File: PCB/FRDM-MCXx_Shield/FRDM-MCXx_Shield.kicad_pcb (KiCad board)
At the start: 4 copper layers, 91.4 x 54.6 mm, 114 parts, among them J2 Conn_01x04_Pin, J3 Conn_01x04_Pin, J4 Conn_01x03_Pin, J5 Conn_01x04_Pin, J6 Conn_01x04_Socket, J7 Conn_01x06_Socket, M1 Motor_Servo, SW1 PEC11L-4120F-N0020, SW2 SW_Push, SW3 SW_Push, U1 M95010-RMN6TP, U2 FXLS8974CF, U4 SN74LV164ADR

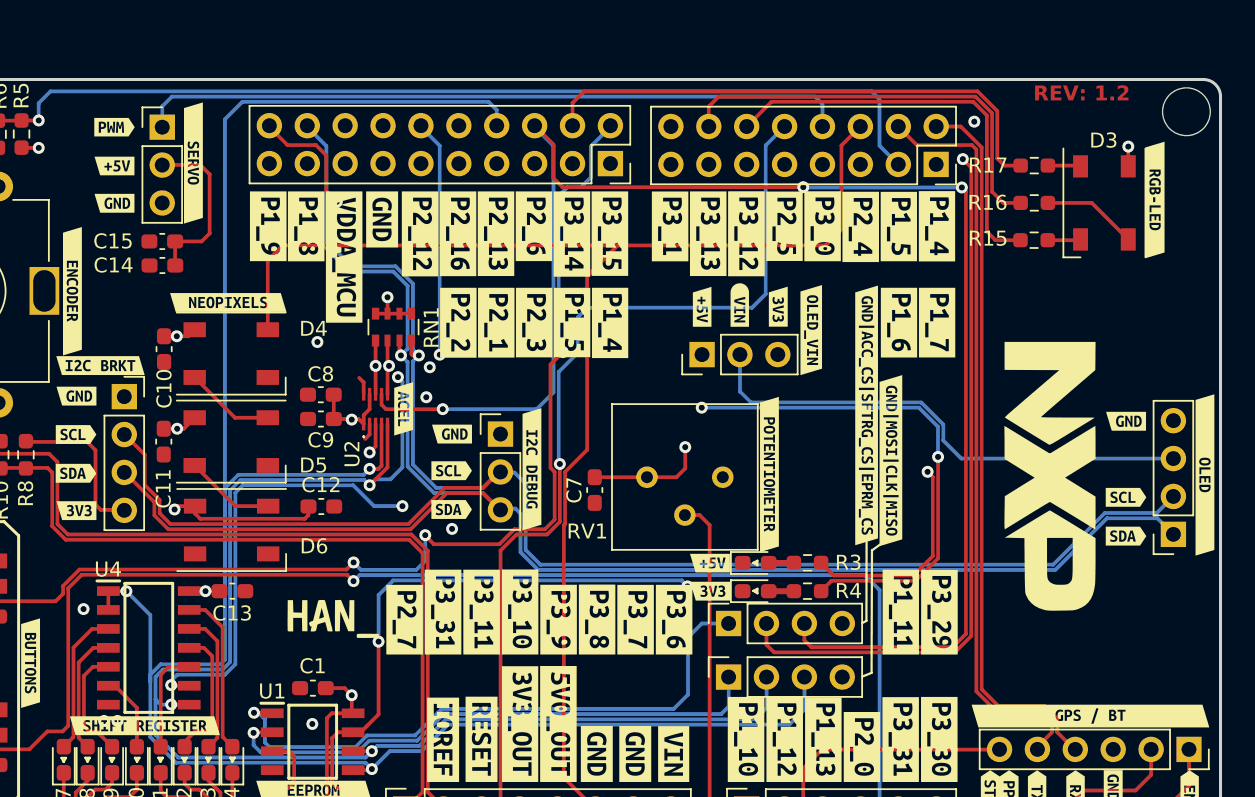
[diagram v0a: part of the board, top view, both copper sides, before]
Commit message: Updated PCB and added bill of materials
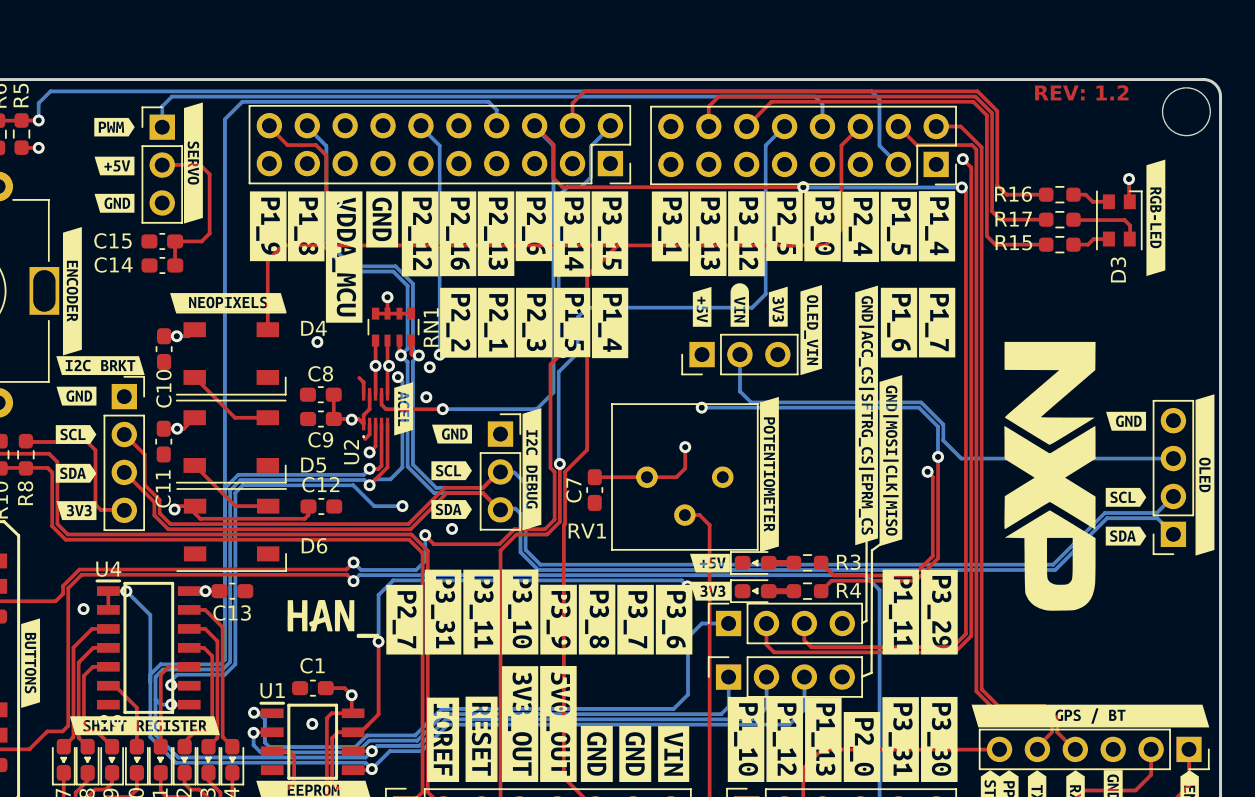
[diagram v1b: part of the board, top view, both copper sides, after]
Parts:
- C14: value 100uF -> 10uF
- D3: footprint LED_SMD:LED_SK6812_PLCC4_5.0x5.0mm_P3.2mm -> LED_SMD:LED_Cree-PLCC4_3.2x2.8mm_CCW
- J4: footprint Connector_PinHeader_2.54mm:PinHeader_1x03_P2.54mm_Vertical -> Connector_PinSocket_2.54mm:PinSocket_1x03_P2.54mm_Vertical
- R15, R16, R17, R3, RN2, RN3: value 420 -> 430
- R4: value 640 -> 680
- moved R17 4.01 mm to (184.9, 68.5)
- moved R16 1.80 mm to (184.9, 66.8)
- moved R15 1.75 mm to (184.9, 70.2)
- moved D3 1.54 mm to (188.8, 68.5)
- moved kibuzzard-65D74BEE 1.20 mm to (191.3, 68.4)
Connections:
- D3 pad 1: Net-(D3-RK) -> +3.3V
- D3 pad 3: +3.3V -> Net-(D3-RK)
- J1 pad B4: /LED_B -> /LED_G
- J1 pad D14: /LED_G -> /LED_B
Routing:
- net /LED_G: track 28.5 -> 39.4 mm
- net /LED_B: track 35.9 -> 31.5 mm
- net Net-(D3-GK): track 6.40 -> 2.70 mm
- net Net-(D3-BK): track 2.14 -> 4.93 mm
- net /LED_R: track 27.4 -> 29.5 mm
- net +3.3V: track 407.2 -> 406.2 mm
- net GND: vias 9 -> 8

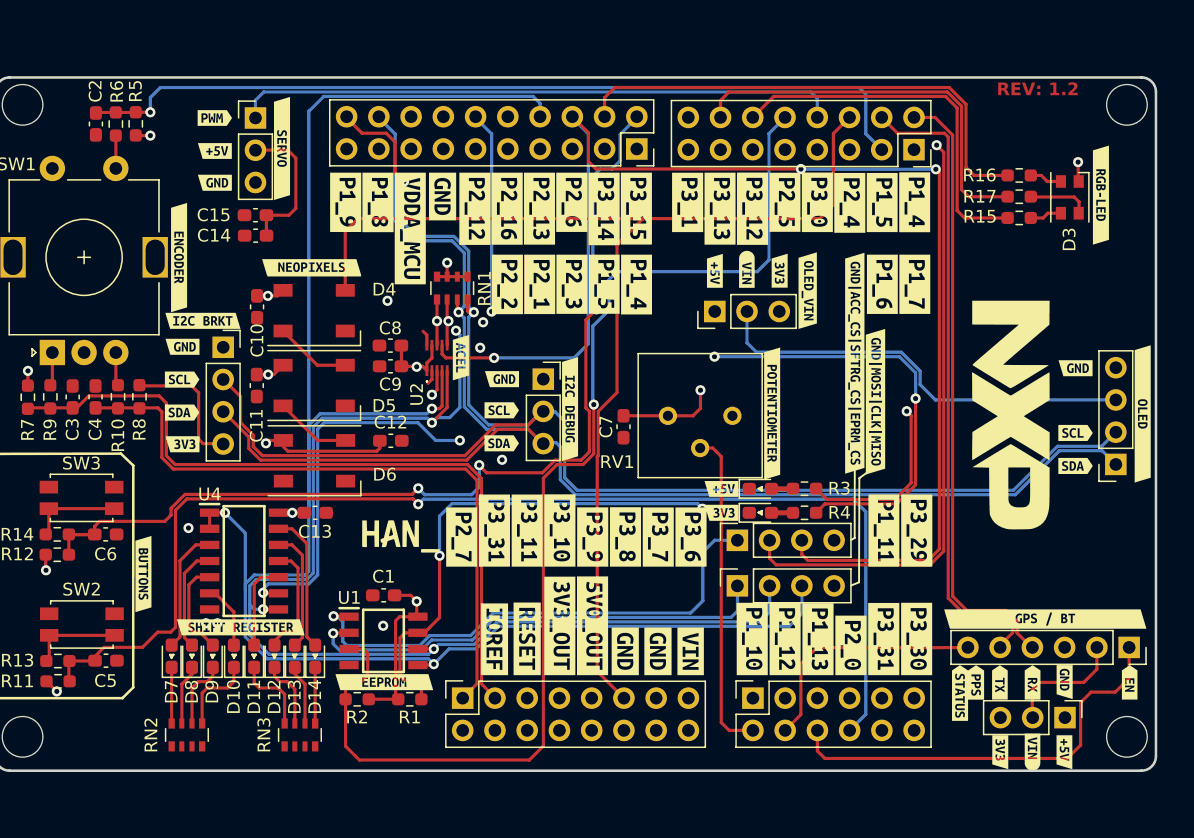
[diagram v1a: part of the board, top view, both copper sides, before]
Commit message: Updated trace spacing and pinout
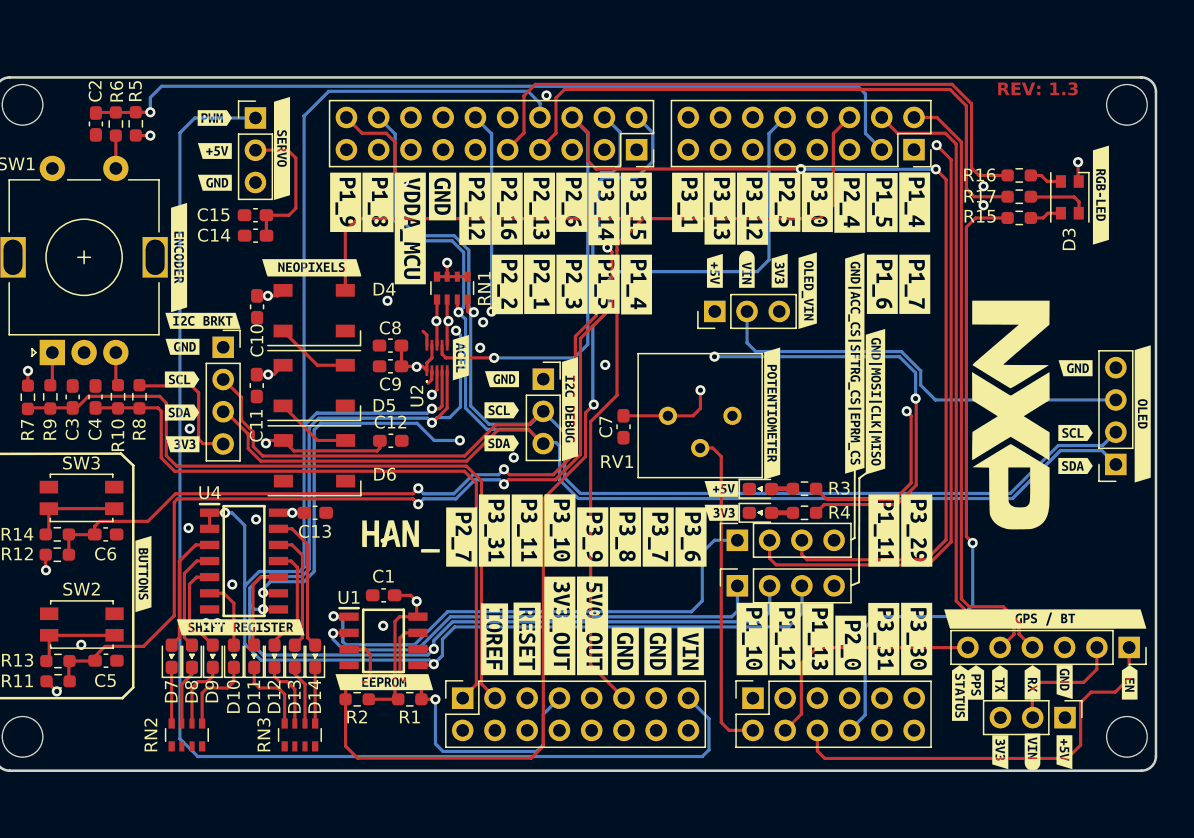
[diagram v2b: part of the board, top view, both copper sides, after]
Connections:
- J1 pad A15: unconnected-(J1A-P3_6-PadA15) -> /SERVO_PWM
- J1 pad A7: unconnected-(J1A-P3_10-PadA7) -> /~{HOLD}
- J1 pad B2: /SWITCH2 -> /SWITCH1
- J1 pad B4: /LED_G -> /SWITCH2
- J1 pad B7: unconnected-(J1B-P2_1-PadB7) -> /LED_B
- J1 pad B9: unconnected-(J1B-P2_2-PadB9) -> /LED_G
- J1 pad C8: /SWITCH1 -> /LED_R
- J1 pad D1: /~{HOLD} -> unconnected-(J1D-P1_7-PadD1)
- J1 pad D12: /LED_R -> unconnected-(J1D-P3_12-PadD12)
- J1 pad D14: /LED_B -> unconnected-(J1D-P3_13-PadD14)
- J1 pad D8: /SERVO_PWM -> unconnected-(J1D-P3_0-PadD8)
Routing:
- net /~{HOLD}: track 81.8 -> 25.5 mm, vias 2 -> 1
- net /SERVO_PWM: track 47.6 -> 101.4 mm
- net /LED_R: track 29.5 -> 51.4 mm, vias 0 -> 1
- net /LED_B: track 31.5 -> 47.7 mm
- net /LED_G: track 39.4 -> 49.1 mm
- net /SWITCH1: track 93.7 -> 86.6 mm, vias 1 -> 3
- net /SPI_MOSI: track 145.8 -> 140.2 mm
- net /SWITCH2: track 76.8 -> 74.4 mm
- net /WRITE_PROT: track 91.9 -> 90.8 mm
- net /SPI_CLK: track 112.7 -> 113.6 mm
- net /SCL: track 121.5 -> 121.0 mm
- net /ACC_INT2: track 69.9 -> 69.4 mm
- net GND: vias 8 -> 16
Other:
- board text added: "REV: 1.3"
- board text removed: "REV: 1.2"

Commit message: Updated V2.0
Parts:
- removed the C13 at (129.4, 93.4)
- removed C5, C6, C7: 100nF, Capacitor_SMD:C_0603_1608Metric_Pad1.08x0.95mm_HandSolder
- removed the C8 at (135.3, 80.2)
- removed the C9 at (135.3, 81.9)
- removed the D1 at (164.5, 91.5)
- removed D10, D11, D12, D13, D14, D7, D8, D9: LED, LED_SMD:LED_0603_1608Metric_Pad1.05x0.95mm_HandSolder
- removed the D2 at (164.5, 93.4)
- removed the D3 at (188.8, 68.5)
- removed the J7 at (193.5, 104.0)
- removed JP2: SolderJumper_3_Open, Connector_PinHeader_2.54mm:PinHeader_1x03_P2.54mm_Vertical
- removed R11, R12: 10k, Resistor_SMD:R_0603_1608Metric_Pad0.98x0.95mm_HandSolder
- removed R13, R14: 1k, Resistor_SMD:R_0603_1608Metric_Pad0.98x0.95mm_HandSolder
- removed R15, R16, R17: 430, Resistor_SMD:R_0603_1608Metric_Pad0.98x0.95mm_HandSolder
- removed the R3 at (167.9, 91.5)
- removed the R4 at (167.9, 93.4)
- removed RN1: 4.7k, Resistor_SMD:R_Array_Convex_4x0603
- removed RN2, RN3: 430, Resistor_SMD:R_Array_Convex_4x0603
- removed RV1: 5k, Potentiometer_THT:Potentiometer_Bourns_3386P_Vertical
- removed SW2, SW3: SW_Push, Button_Switch_SMD:SW_SPST_EVQP2
- removed U2: FXLS8974CF, SamacSys_Parts:FXLS8974CF
- removed U4: SN74LV164ADR, SamacSys_Parts:SOIC127P600X175-14N
- removed kibuzzard-65C7C6A4: G***, kibuzzard-65C7C6A4
- removed kibuzzard-65C7C6B6: G***, kibuzzard-65C7C6B6
- removed kibuzzard-65C7C6CC: G***, kibuzzard-65C7C6CC
- removed kibuzzard-65C7CAB6: G***, kibuzzard-65C7CAB6
- removed kibuzzard-65C7CCAF: G***, kibuzzard-65C7CCAF
- removed kibuzzard-65C7CD45: G***, kibuzzard-65C7CD45
- removed kibuzzard-65D5B8C7: G***, kibuzzard-65D5B8C7
- removed kibuzzard-65D5B8D9: G***, kibuzzard-65D5B8D9
- removed kibuzzard-65D5B8E6: G***, kibuzzard-65D5B8E6
- removed kibuzzard-65D5B934: G***, kibuzzard-65D5B934
- removed kibuzzard-65D5B943: G***, kibuzzard-65D5B943
- removed kibuzzard-65D5B980: G***, kibuzzard-65D5B980
- removed kibuzzard-65D5C5A7: G***, kibuzzard-65D5C5A7
- removed kibuzzard-65D5C99D: G***, kibuzzard-65D5C99D
- removed kibuzzard-65D74BEE: G***, kibuzzard-65D74BEE
- removed kibuzzard-65D74C28: G***, kibuzzard-65D74C28
- removed kibuzzard-65D9F210: G***, kibuzzard-65D9F210
- added J2: Conn_02x10_Odd_Even, Connector_PinHeader_2.54mm:PinHeader_2x10_P2.54mm_Vertical, B.Cu at (154.7, 64.8)
- added J3: Conn_02x06_Odd_Even, Connector_PinHeader_2.54mm:PinHeader_2x06_P2.54mm_Vertical, B.Cu at (163.9, 108.0)
- added J4: Conn_02x08_Odd_Even, Connector_PinHeader_2.54mm:PinHeader_2x08_P2.54mm_Vertical, B.Cu at (176.6, 64.8)
- added SSD1306: 128x64OLED, OLED:128x64OLED, F.Cu at (167.2, 82.2)
- added U3: 74HC595, Package_SO:TSSOP-16_4.4x5mm_P0.65mm, F.Cu at (223.0, 104.3)
- J1: value ~ -> Conn_02x08_Odd_Even; footprint User:MCX-A153_Shield_Template -> Connector_PinHeader_2.54mm:PinHeader_2x08_P2.54mm_Vertical; moved to B.Cu
- U1: footprint SamacSys_Parts:SOIC127P600X175-8N -> SamacSys:SOIC127P600X175-8N
- moved J1 54.4 mm to (141.0, 108.0), turned to -90 degrees
- moved REF** 17.0 mm to (174.0, 70.9)
- moved REF** 17.0 mm to (165.8, 70.8)
- renumbered C12 to C10, C14 to C12, C15 to C13, C10 to C8, C11 to C9, D4 to D1, D5 to D2, D6 to D3, J2 to J5, J3 to J6, J4 to J7, J5 to J8, J6 to J9, R5 to R3, R6 to R4, R7 to R5, R8 to R6, R9 to R7, R10 to R8
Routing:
- net +3.3V: track 405.9 -> 313.9 mm, vias 14 -> 8
- net /ACC_INT2: track 69.4 -> 0.00 mm, vias 1 -> 0
- net /ACC_INT1: track 69.4 -> 0.00 mm, vias 1 -> 0
- net +5V: track 184.0 -> 149.1 mm
- net /BT_EN: track 33.4 -> 21.6 mm
- net /Actuators/LED_H: track 11.0 -> 0.00 mm
- net /Actuators/LED_A: track 9.77 -> 0.00 mm
- net Net-(J7-Pin_2): track 9.68 -> 0.00 mm
- net /Actuators/LED_G: track 9.55 -> 0.00 mm
- net /Actuators/LED_F: track 8.67 -> 0.00 mm
- net /Actuators/LED_B: track 8.29 -> 0.00 mm
- net /SWITCH1: track 86.6 -> 78.5 mm
- net /RX: track 48.2 -> 40.5 mm
- net /Actuators/LED_C: track 7.68 -> 0.00 mm
- net /TX: track 50.3 -> 42.7 mm
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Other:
- board size 91.4 x 54.6 mm -> 51.1 x 54.7 mm
- board text added: "REV: 2.0"
- board text removed: "REV: 1.3"

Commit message: Updated PCB
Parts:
- removed C13: 100nF, Capacitor_SMD:C_0603_1608Metric_Pad1.08x0.95mm_HandSolder
- removed the J1 at (141.0, 108.0)
- removed the J3 at (163.9, 108.0)
- removed J9: Conn_01x04_Socket, Connector_PinSocket_2.54mm:PinSocket_1x04_P2.54mm_Vertical
- added C11: 100nF, Capacitor_SMD:C_0805_2012Metric_Pad1.18x1.45mm_HandSolder, F.Cu at (141.3, 110.0)
- added C5: 10nF, Capacitor_SMD:C_0805_2012Metric_Pad1.18x1.45mm_HandSolder, F.Cu at (157.5, 88.9)
- added C6: 100nF, Capacitor_SMD:C_0805_2012Metric_Pad1.18x1.45mm_HandSolder, F.Cu at (165.6, 102.7)
- added C7: 100nF, Capacitor_SMD:C_0805_2012Metric_Pad1.18x1.45mm_HandSolder, F.Cu at (172.2, 102.7)
- added D10: SP0503BAHT, Package_TO_SOT_SMD:SOT-143, B.Cu at (139.7, 80.0)
- added D11: SP0503BAHT, Package_TO_SOT_SMD:SOT-143, B.Cu at (148.4, 80.0)
- added D12: SP0503BAHT, Package_TO_SOT_SMD:SOT-143, F.Cu at (157.3, 101.6)
- added D13: SP0503BAHT, Package_TO_SOT_SMD:SOT-143, B.Cu at (152.9, 107.9)
- added D14: SK6812, LED_SMD:LED_SK6812_PLCC4_5.0x5.0mm_P3.2mm, F.Cu at (164.7, 107.5)
- added D15: SK6812, LED_SMD:LED_SK6812_PLCC4_5.0x5.0mm_P3.2mm, F.Cu at (171.3, 107.5)
- added D16: SK6812, LED_SMD:LED_SK6812_PLCC4_5.0x5.0mm_P3.2mm, F.Cu at (177.9, 107.5)
- added D4: LED, LED_SMD:LED_0805_2012Metric_Pad1.15x1.40mm_HandSolder, F.Cu at (179.5, 90.9)
- added D5: LED, LED_SMD:LED_0805_2012Metric_Pad1.15x1.40mm_HandSolder, F.Cu at (176.3, 98.7)
- added D6: LED, LED_SMD:LED_0805_2012Metric_Pad1.15x1.40mm_HandSolder, F.Cu at (168.5, 101.9)
- added D7: LED, LED_SMD:LED_0805_2012Metric_Pad1.15x1.40mm_HandSolder, F.Cu at (160.8, 98.7)
- added D8: LED, LED_SMD:LED_0805_2012Metric_Pad1.15x1.40mm_HandSolder, F.Cu at (157.5, 90.9)
- added D9: SP0503BAHT, Package_TO_SOT_SMD:SOT-143, B.Cu at (144.0, 80.0)
- added J2: Conn_02x06_Odd_Even, Connector_PinHeader_2.54mm:PinHeader_2x06_P2.54mm_Vertical, B.Cu at (163.7, 112.8)
- added J4: Conn_02x08_Odd_Even, Connector_PinHeader_2.54mm:PinHeader_2x08_P2.54mm_Vertical, B.Cu at (140.8, 112.8)
- added RN1: 4.7k, Resistor_SMD:R_Array_Convex_4x1206, F.Cu at (132.7, 81.6)
- added RN2: 1k, Resistor_SMD:R_Array_Convex_4x1206, F.Cu at (168.5, 75.5)
- added RN3: 1k, Resistor_SMD:R_Array_Convex_4x1206, F.Cu at (177.4, 75.5)
- added TP1: 5001, SamacSys:5000, F.Cu at (179.8, 68.1)
- added TP2: 5001, SamacSys:5000, F.Cu at (161.1, 102.0)
- added TP3: 5001, SamacSys:5000, F.Cu at (157.3, 82.3)
- added TP4: 5001, SamacSys:5000, F.Cu at (137.4, 106.9)
- added TP5: 5001, SamacSys:5000, F.Cu at (158.5, 105.0)
- added TP6: 5001, SamacSys:5000, F.Cu at (158.5, 109.4)
- added U2: M95010-RMN6TP, SamacSys:SOIC127P600X175-8N, F.Cu at (146.7, 74.5)
- C1, C2, C3, C8, C9: footprint Capacitor_SMD:C_0603_1608Metric_Pad1.08x0.95mm_HandSolder -> Capacitor_SMD:C_0805_2012Metric_Pad1.18x1.45mm_HandSolder
- C10: value 100nF -> 10uF; footprint Capacitor_SMD:C_0603_1608Metric_Pad1.08x0.95mm_HandSolder -> Capacitor_SMD:C_0805_2012Metric_Pad1.18x1.45mm_HandSolder
- C12: value 10uF -> 100nF; footprint Capacitor_SMD:C_0603_1608Metric_Pad1.08x0.95mm_HandSolder -> Capacitor_SMD:C_0805_2012Metric_Pad1.18x1.45mm_HandSolder
- C4: value 100nF -> 10nF; footprint Capacitor_SMD:C_0603_1608Metric_Pad1.08x0.95mm_HandSolder -> Capacitor_SMD:C_0805_2012Metric_Pad1.18x1.45mm_HandSolder
- D1, D2, D3: value SK6812 -> LED; footprint LED_SMD:LED_SK6812_PLCC4_5.0x5.0mm_P3.2mm -> LED_SMD:LED_0805_2012Metric_Pad1.15x1.40mm_HandSolder
- J5: value Conn_01x04_Pin -> Conn_01x04_Socket
- J6, J8: footprint Connector_PinSocket_2.54mm:PinSocket_1x04_P2.54mm_Vertical -> Connector_PinHeader_2.54mm:PinHeader_1x04_P2.54mm_Vertical
- J7: value Conn_01x03_Pin -> Conn_01x04_Pin; footprint Connector_PinSocket_2.54mm:PinSocket_1x03_P2.54mm_Vertical -> Connector_PinHeader_2.54mm:PinHeader_1x04_P2.54mm_Vertical
- JP1: footprint Connector_PinHeader_2.54mm:PinHeader_1x03_P2.54mm_Vertical -> Jumper:SolderJumper-3_P2.0mm_Open_TrianglePad1.0x1.5mm; moved to B.Cu
- R1, R3: footprint Resistor_SMD:R_0603_1608Metric_Pad0.98x0.95mm_HandSolder -> Resistor_SMD:R_0805_2012Metric_Pad1.20x1.40mm_HandSolder
- R2, R5, R6: value 10k -> 1k; footprint Resistor_SMD:R_0603_1608Metric_Pad0.98x0.95mm_HandSolder -> Resistor_SMD:R_0805_2012Metric_Pad1.20x1.40mm_HandSolder
- R4, R7, R8: value 1k -> 10k; footprint Resistor_SMD:R_0603_1608Metric_Pad0.98x0.95mm_HandSolder -> Resistor_SMD:R_0805_2012Metric_Pad1.20x1.40mm_HandSolder
- SW1: value PEC11L-4120F-N0020 -> EC12D1524406; footprint Rotary_Encoder:RotaryEncoder_Alps_EC11E-Switch_Vertical_H20mm -> SamacSys:EC12D1564404
- U1: value M95010-RMN6TP -> 74HC595; footprint SamacSys:SOIC127P600X175-8N -> Package_SO:TSSOP-16_4.4x5mm_P0.65mm
- U3: value 74HC595 -> LM35-D; footprint Package_SO:TSSOP-16_4.4x5mm_P0.65mm -> Package_SO:SOIC-8_3.9x4.9mm_P1.27mm
- moved kibuzzard-65C7C5A7 170.9 mm to (47.4, 177.2)
- moved kibuzzard-65C7C751 170.9 mm to (47.4, 182.3)
- moved kibuzzard-65C7C77A 170.9 mm to (47.4, 184.9)
- moved kibuzzard-65D9ED05 170.9 mm to (52.7, 180.8)
- moved kibuzzard-65D9F158 155.2 mm to (34.4, 156.7)
- moved kibuzzard-65C7C73C 155.2 mm to (29.3, 156.7)
- moved kibuzzard-65D9F1EE 155.2 mm to (31.8, 156.6)
- moved kibuzzard-65D9F4C2 155.2 mm to (36.6, 158.2)
- moved kibuzzard-65D9F92F 145.9 mm to (67.7, 183.7)
- moved kibuzzard-65D9F962 145.9 mm to (69.3, 186.7)
- moved kibuzzard-65C7C452 115.8 mm to (23.2, 123.4)
- moved kibuzzard-65C7C5C0 115.8 mm to (23.2, 126.0)
- moved kibuzzard-65C7C5CF 115.8 mm to (23.2, 128.5)
- moved kibuzzard-65C7CF1C 115.8 mm to (28.5, 125.8)
- moved kibuzzard-65C7C751 112.3 mm to (57.1, 156.3)
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- renumbered J4 to J1, J2 to J3
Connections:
- C10 pad 1: +3.3V -> GND
- C10 pad 2: GND -> +5V
- C12 pad 1: GND -> +3.3V
- C12 pad 2: +5V -> GND
- C2 pad 1: /ENC_SW -> GND
- C2 pad 2: GND -> +3.3V
- C3 pad 1: /ENC_A -> /ENC_SW
- C4 pad 1: /ENC_B -> /ENC_A
- D1 pad 2: /LED_NEOPIXEL -> Net-(D1-A)
- D2 pad 2: Net-(D1-DOUT) -> Net-(D2-A)
- D3 pad 2: Net-(D2-DOUT) -> Net-(D3-A)
- J1 pad 14: unconnected-(J4-Pin_14-Pad14) -> /SERVO_PWM
- J1 pad 16: /~{SHIFTREG_CS} -> /~{SHIFTREG_RST}
- J1 pad 2: /RX -> unconnected-(J1-Pin_2-Pad2)
- J1 pad 4: /TX -> unconnected-(J1-Pin_4-Pad4)
- J1 pad 6: /LED_NEOPIXEL -> unconnected-(J1-Pin_6-Pad6)
- J3 pad 2: /SWITCH1 -> unconnected-(J3-Pin_2-Pad2)
- J3 pad 3: /ACC_INT2 -> unconnected-(J3-Pin_3-Pad3)
- J3 pad 4: /SWITCH2 -> unconnected-(J3-Pin_4-Pad4)
- J3 pad 5: /ACC_INT1 -> unconnected-(J3-Pin_5-Pad5)
- J3 pad 6: /~{ACC_CS} -> /~{SHIFTREG_CS}
- J3 pad 7: /LED_B -> unconnected-(J3-Pin_7-Pad7)
- J3 pad 9: /LED_G -> unconnected-(J3-Pin_9-Pad9)
- J5 pad 1: /~{EEPROM_CS} -> /SDA
- J5 pad 2: /~{SHIFTREG_CS} -> /SCL
- J5 pad 3: /~{ACC_CS} -> Net-(J5-Pin_3)
- J6 pad 1: /SPI_MISO -> /~{EEPROM_CS}
- J6 pad 2: /SPI_CLK -> /~{SHIFTREG_CS}
- J6 pad 3: /SPI_MOSI -> /~{SHIFTREG_RST}
- J7 pad 1: GND -> /SPI_MOSI
- J7 pad 2: /SCL -> /SPI_CLK
- J7 pad 3: /SDA -> /SPI_MISO
- J8 pad 1: GND -> +3.3V
- J8 pad 2: /SCL -> /SDA
- J8 pad 3: /SDA -> /SCL
- J8 pad 4: +3.3V -> GND
- JP1 pad 1: +5V -> +3.3V
- JP1 pad 2: Net-(J9-Pin_3) -> Net-(J5-Pin_3)
- JP1 pad 3: +3.3V -> +5V
- R1 pad 1: +3.3V -> /ENC_SW
- R1 pad 2: /~{HOLD} -> +3.3V
- R2 pad 1: +3.3V -> /HMI/ENC_SW_RAW
- R2 pad 2: /WRITE_PROT -> /ENC_SW
- R3 pad 1: /ENC_SW -> /ENC_A
- R4 pad 1: /HMI/ENC_SW_RAW -> /ENC_B
- R4 pad 2: /ENC_SW -> +3.3V
- R5 pad 1: /ENC_A -> /HMI/ENC_A_RAW
- R5 pad 2: +3.3V -> /ENC_A
- R6 pad 1: /ENC_B -> /HMI/ENC_B_RAW
- R6 pad 2: +3.3V -> /ENC_B
- R7 pad 1: /HMI/ENC_A_RAW -> +3.3V
- R7 pad 2: /ENC_A -> Net-(U2-~{HOLD})
- R8 pad 1: /HMI/ENC_B_RAW -> +3.3V
- R8 pad 2: /ENC_B -> /WRITE_PROT
- U1 pad 1: /~{EEPROM_CS} -> Net-(RN2C-R3.2)
- U1 pad 2: /SPI_MISO -> Net-(RN2B-R2.2)
- U1 pad 3: /WRITE_PROT -> Net-(RN2A-R1.2)
- U1 pad 4: GND -> Net-(RN3A-R1.2)
- U1 pad 5: /SPI_MOSI -> Net-(RN3B-R2.2)
- U1 pad 6: /SPI_CLK -> Net-(RN3C-R3.2)
- U1 pad 7: /~{HOLD} -> Net-(RN3D-R4.2)
- U1 pad 8: +3.3V -> GND
- U3 pad 1: unconnected-(U3-QB-Pad1) -> /ADC_OUT
- U3 pad 4: unconnected-(U3-QE-Pad4) -> GND
- U3 pad 8: unconnected-(U3-GND-Pad8) -> +3.3V
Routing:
- net +3.3V: track 313.9 -> 37.0 mm, vias 8 -> 0
- net /~{SHIFTREG_CS}: track 143.5 -> 0.00 mm, vias 2 -> 0
- net +5V: track 149.1 -> 7.32 mm, vias 2 -> 0
- net /SPI_MOSI: track 134.0 -> 7.53 mm, vias 1 -> 0
- net /~{ACC_CS}: track 100.7 -> 0.00 mm, vias 2 -> 0
- net /SPI_CLK: track 107.8 -> 7.81 mm, vias 3 -> 0
- net /SERVO_PWM: track 101.4 -> 3.53 mm
- net /SDA: track 115.1 -> 28.4 mm, vias 1 -> 0
- net /WRITE_PROT: track 90.8 -> 4.17 mm, vias 1 -> 0
- net /SCL: track 121.0 -> 36.1 mm, vias 2 -> 0
- net /SWITCH1: track 78.5 -> 0.00 mm, vias 3 -> 0
- net /SPI_MISO: track 89.3 -> 13.2 mm, vias 1 -> 0
- net /LED_NEOPIXEL: track 92.0 -> 16.6 mm
- net /SWITCH2: track 69.6 -> 0.00 mm, vias 3 -> 0
- net /~{EEPROM_CS}: track 68.7 -> 0.00 mm, vias 1 -> 0
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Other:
- board size 51.1 x 54.7 mm -> 54.3 x 54.7 mm
